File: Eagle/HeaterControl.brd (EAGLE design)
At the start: 24.1 x 37.6 mm, 27 parts, among them Q1 P-FET

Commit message: Rev 1
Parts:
- removed U$9: OMROM_TH, CuriousTech:OMROM_TH
- added LEFT, RIGHT: OMROM_TH, CuriousTech:OMROM_TH
- C1: value 1uF -> 0.1uF
- R5: value 10K -> 1K
- U$8: value OMROM_TH -> SMD-PAD1; device CuriousTech:OMROM_TH -> CuriousTech:SMD-PAD1
- moved U$8 8.92 mm to (13.5, 2.03), flipped to the bottom, turned to 90 degrees
- moved U$11 2.29 mm to (16.0, 2.03)
- moved U$2 1.52 mm to (19.1, 2.03)
- moved U$3 1.52 mm to (21.6, 2.03)
- moved U$6 1.52 mm to (24.1, 2.03)
- moved U$7 0.25 mm to (10.9, 2.03)
- renumbered C3 to C1
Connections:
- net 3V3: now also U$8.>NAME
- net GND: now also LEFT.P2, LEFT.P4, RIGHT.P2, RIGHT.P4; no longer U$8.P2, U$8.P4, U$9.P2, U$9.P4
- net IO13: now also RIGHT.P1; no longer U$9.P1
- net IO14: now also LEFT.P3; no longer U$8.P3
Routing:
- net 3V3: track 86.9 -> 95.4 mm
- net N$1: track 10.3 -> 11.8 mm
- net IO13: track 4.80 -> 5.43 mm
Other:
- board size 24.1 x 37.6 mm -> 25.7 x 37.6 mm
- board text added: "DS18B20 IO16"
- board text added: "IO14"
- board text removed: "IO16"
- board text removed: "Water Sense IO16"

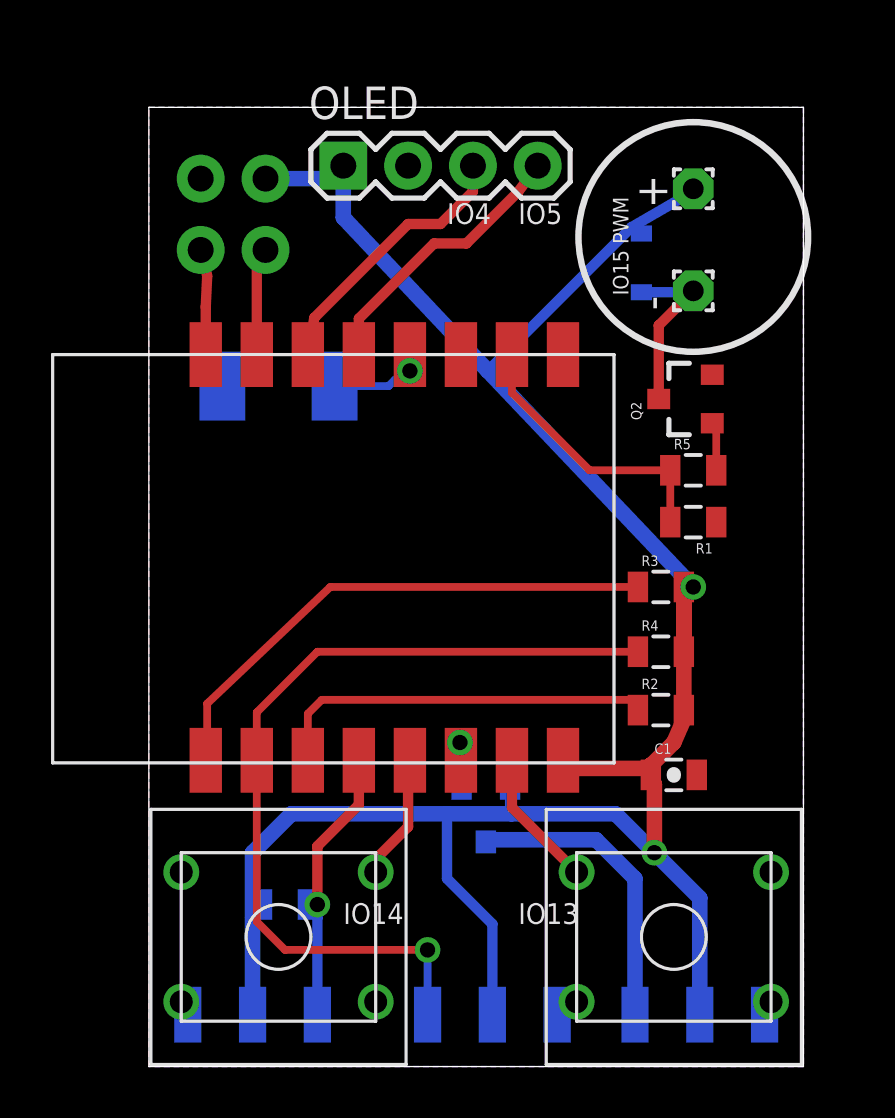
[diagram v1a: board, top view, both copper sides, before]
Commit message: Rev 1 buttons/screen aligned
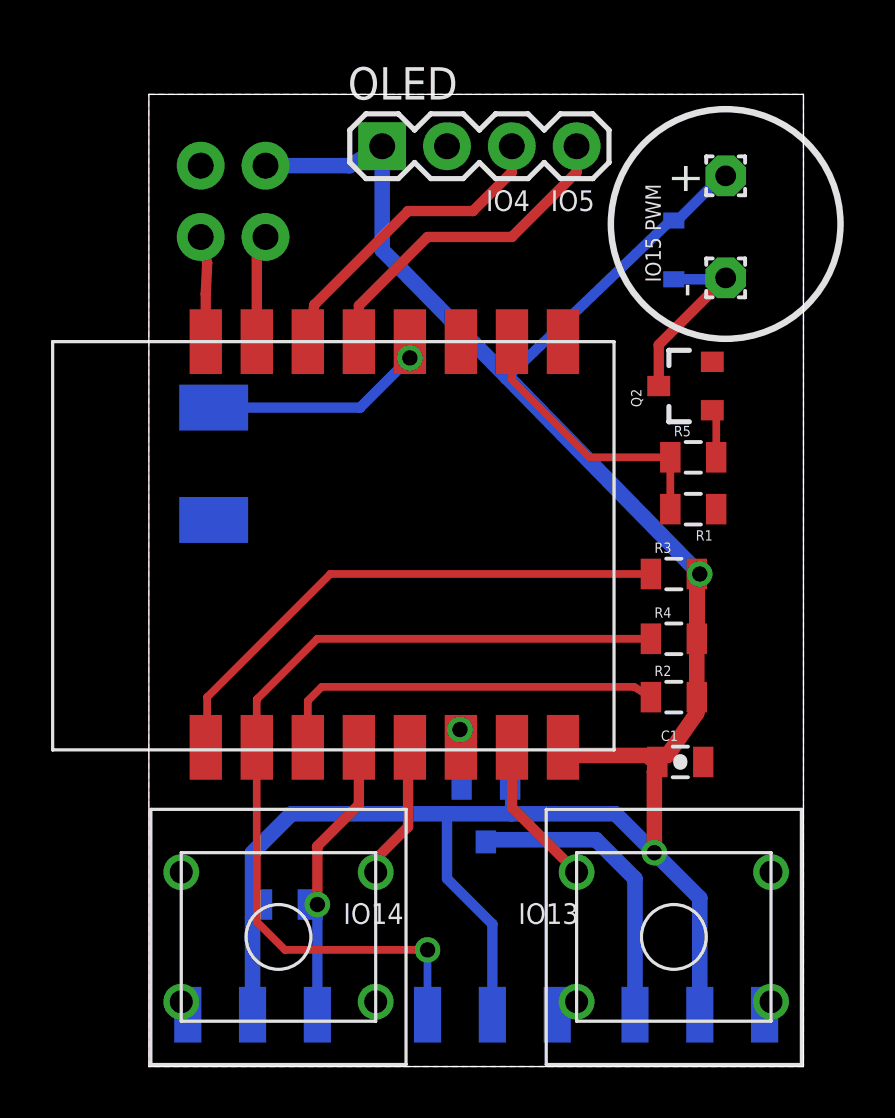
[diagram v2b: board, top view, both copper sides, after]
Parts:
- moved FLASH 3.97 mm to (2.54, 23.6), turned to 90 degrees
- moved OLED 1.70 mm to (9.14, 36.1)
- moved + 1.37 mm to (22.6, 34.9)
- moved - 1.37 mm to (22.6, 30.9)
- moved D1 1.37 mm to (20.6, 32.0)
- moved R2 0.72 mm to (20.6, 14.5)
- moved R3 0.72 mm to (20.6, 19.3)
- moved R4 0.72 mm to (20.6, 16.8)
- moved C1 0.57 mm to (20.8, 11.9)
- moved . 0.51 mm to (2.03, 32.5)
- moved Q2 0.51 mm to (21.1, 26.7)
- moved R1 0.51 mm to (21.3, 21.8)
- moved R5 0.51 mm to (21.3, 23.9)
- moved U$1 0.51 mm to (18.2, 12.4)
- moved +__- 0.51 mm to (4.57, 35.3)
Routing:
- net IO0: track 3.84 -> 9.14 mm
- net 3V3: track 95.4 -> 98.8 mm
- net N$9: track 11.0 -> 13.1 mm
- net N$3: track 10.7 -> 12.4 mm
- net ADC: track 33.8 -> 34.8 mm
- net N$4: track 6.88 -> 7.41 mm
- net IO16: track 11.8 -> 12.3 mm
- net IO14: track 4.94 -> 5.45 mm
- net IO13: track 5.43 -> 5.94 mm
- net IO12: track 2.51 -> 3.02 mm
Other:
- board size 25.7 x 37.6 mm -> 25.7 x 38.1 mm
